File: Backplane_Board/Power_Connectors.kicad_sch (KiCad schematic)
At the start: 15 parts, among them J1 Conn_01x02_Pin, J10 Conn_01x02_Pin, J11 Conn_01x02_Pin, J12 Conn_01x02_Pin, J13 Conn_01x02_Pin, J14 Conn_01x02_Pin, J15 Conn_01x02_Pin, J16 Conn_01x02_Pin, J2 Conn_01x02_Pin, J4 Conn_01x02_Pin, J5 Conn_01x02_Pin, J6 Conn_01x02_Pin, J7 Conn_01x02_Pin, J8 Conn_01x02_Pin, J9 Conn_01x02_Pin

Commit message: add rerevised esc board and rough backplane schmatic
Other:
- company: (none) -> Cabrillo Robtics
- title: (none) -> Backplane_Board
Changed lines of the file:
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@@
 	(generator_version "8.0")
 	(paper "A4")
+	(title_block
+		(title "Backplane_Board")
+		(date "2024-09-30")
+		(rev "1")
+		(company "Cabrillo Robtics")
+		(comment 1 "LaserShark Backplane PCB")
+	)
 	(wire
 		(pts

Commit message: back plane board ready for review
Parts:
- added C11, C7, C8: 330 uF, 220UF CAP:CAP_16SVPG330MX, symbol Device:C_Polarized_Small_US
- added D3: LED, symbol Device:LED
- added J18, J19, J20, J3: Conn_01x02_Pin, symbol Connector:Conn_01x02_Pin
- added R10, R15: DNP, symbol Device:R
- added R17: 10K, symbol Device:R
- added U6: PKU3511SPI, PKU 3500S_FPM, symbol PKU3511SPI:PKU3511SPI
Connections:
- net +12V: now also J3.2 (Pin_2), U6.1 (+VIN)
- net +5V: now also C11.1, C7.1, C8.1, D3.2 (A), J18.2 (Pin_2), J19.2 (Pin_2), J20.2 (Pin_2), R10.1, U6.7 (SENSE), U6.8 (+VO)
- net GND: now also C11.2, C7.2, C8.2, J18.1 (Pin_1), J19.1 (Pin_1), J20.1 (Pin_1), J3.1 (Pin_1), R15.2, R17.2, U6.2 (ON/OFF), U6.3 (-VIN), U6.4 (-VO), U6.5 (SENSE)
- new net: R10.2, R15.1, U6.6 (TRIM)
- new net: D3.1 (K), R17.1
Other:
- note added: "12V Clean Power Bus External Power Connections"
- note added: "12V ESC Power Bus External Power Connections"
- note added: "5V Power Bus"
- note added: "5V Power Bus Cap Banks and status LEDs"
- note added: "5V Power Bus External Power Connections"
- note added: "Input Test Accesses"
- note added: "fuse?"
- note removed: "This bus is used to power anything that could be dangrous things go crazy ESC Boards, Tooling..."
- moved on the sheet: J1, J11, J16, J2, J4, J5, J6

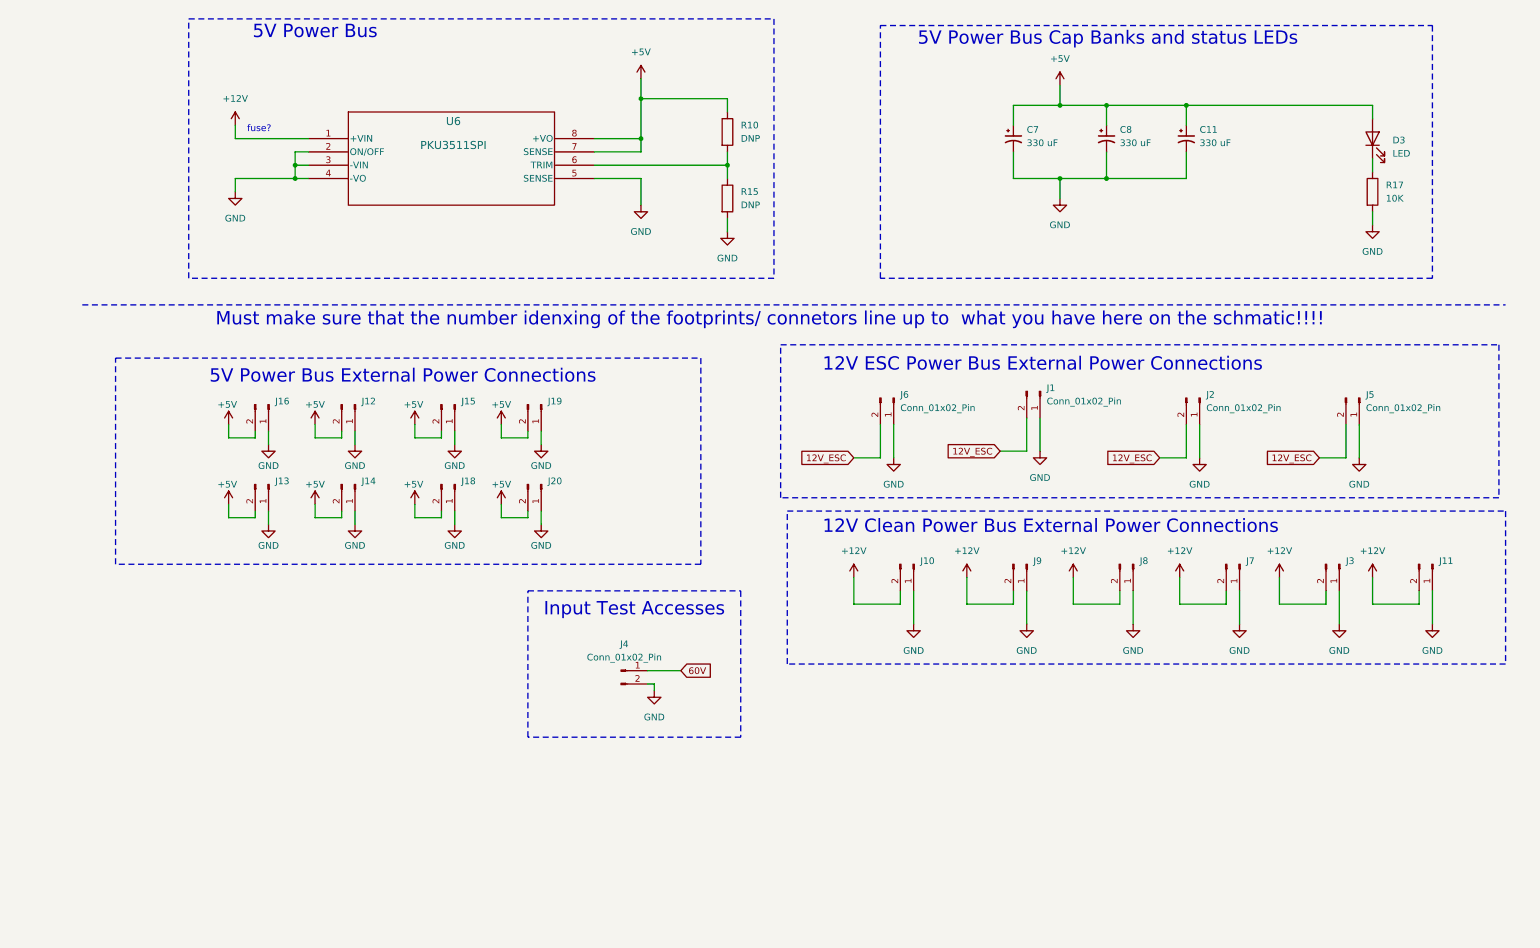
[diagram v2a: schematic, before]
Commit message: added pico and 5v killSW
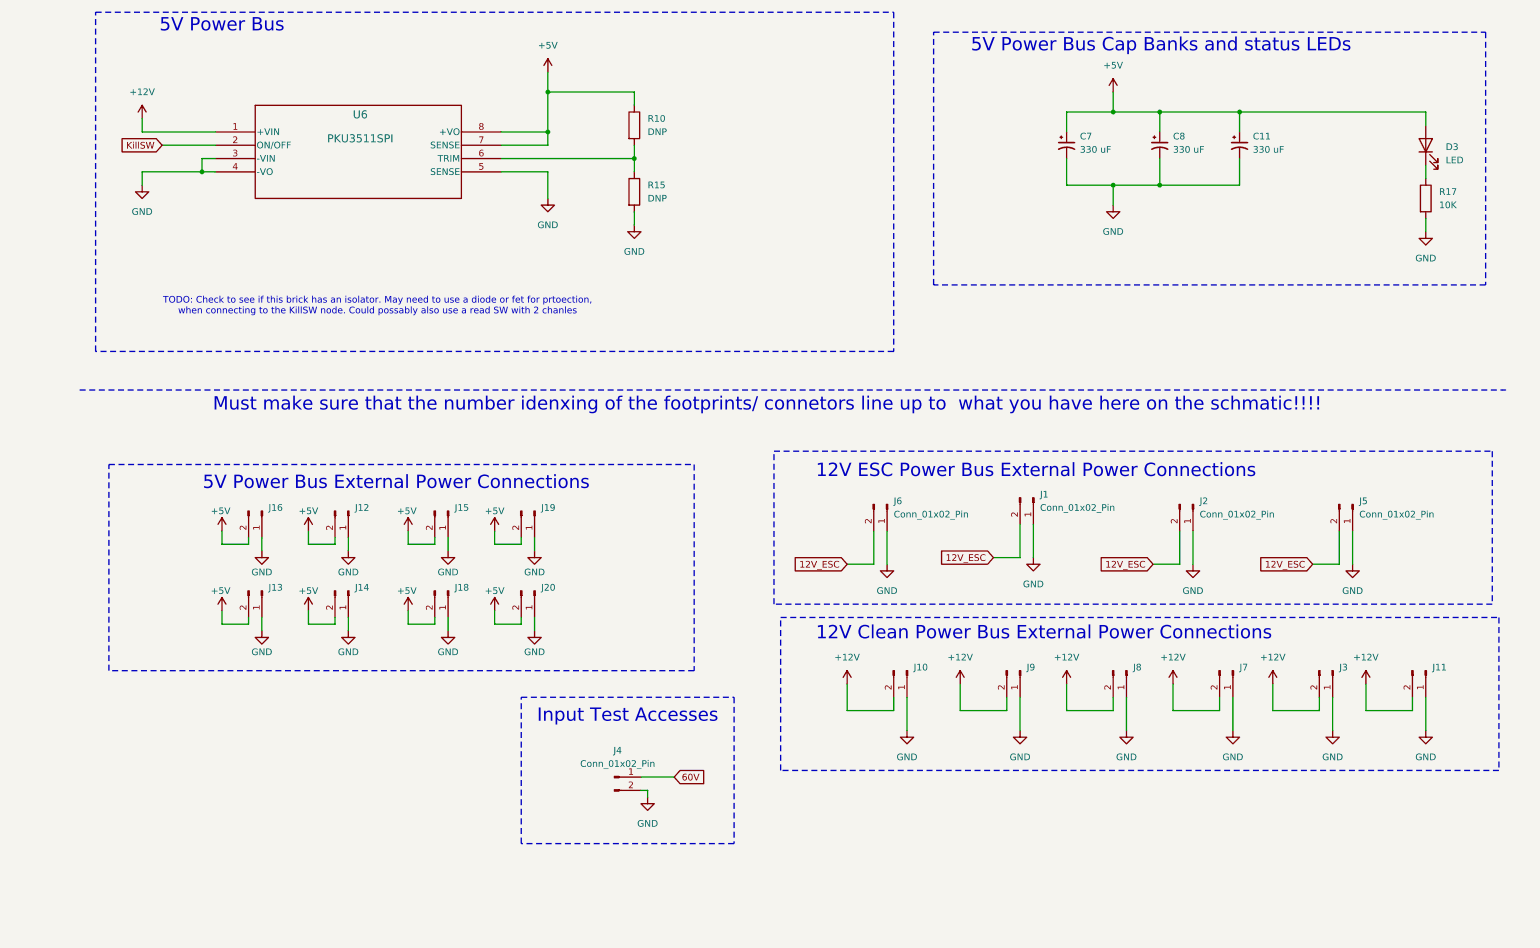
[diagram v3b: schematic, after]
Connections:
- net GND: no longer U6.2 (ON/OFF)
- new net KillSW: U6.2 (ON/OFF)
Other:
- note added: "TODO: Check to see if this brick has an isolator. May need to use a diode or fet for prtoection, when connecting to the KillSW node. Could possably also use a read SW with 2 chanles"
- note removed: "fuse?"
- moved on the sheet: C11, C7, C8, D3, J1, J10, J11, J12, J13, J14, J15, J16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

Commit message: added more pico stuff
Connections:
- net KillSW is gone; now on net GND: U6.2 (ON/OFF)
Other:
- note added: "TODO: Check to see if this brick has an isolator. May need to use a diode or fet for prtoection, when connecting to the KillSW node. Could possably also use a read SW with 2 chanles Note: Currently aways on. We do not want to kill the full buss in the event that the kill swtich is pulled"
- note removed: "TODO: Check to see if this brick has an isolator. May need to use a diode or fet for prtoection, when connecting to the KillSW node. Could possably also use a read SW with 2 chanles"
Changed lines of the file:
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@@
+	)
+	(junction
+		(at 35.56 41.91)
+		(diameter 0)
+		(color 0 0 0 0)
 	)
 	(junction
@@
 	(wire
 		(pts
+			(xy 35.56 39.37) (xy 35.56 41.91)
+		)
+		(stroke
+			(width 0)
+			(type default)
+		)
+	)
+	(wire
+		(pts
 			(xy 44.45 130.81) (xy 44.45 129.54)
+		)
+		(stroke
+			(width 0)
+			(type default)
+		)
+	)
+	(wire
+		(pts
+			(xy 38.1 39.37) (xy 35.56 39.37)
 		)
 		(stroke
@@
 		(pts
 			(xy 269.24 53.34) (xy 269.24 55.88)
-		)
-		(stroke
-			(width 0)
-			(type default)
-		)
-	)
-	(wire
-		(pts
-			(xy 27.94 39.37) (xy 38.1 39.37)
 		)
 		(stroke
@@
 		)
 	)
-	(text "TODO: Check to see if this brick has an isolator. May need to use a diode or fet for prtoection,\nwhen connecting to the KillSW node. Could possably also use a read SW with 2 chanles"
+	(text "TODO: Check to see if this brick has an isolator. May need to use a diode or fet for prtoection,\nwhen connecting to the KillSW node. Could possably also use a read SW with 2 chanles\n\nNote: Currently aways on. We do not want to kill the full buss in the event that the kill swtich is pulled"
 		(exclude_from_sim no)
-		(at 69.088 70.104 0)
+		(at 45.212 68.58 0)
 		(effects
 			(font
@@
 				(color 255 52 89 1)
 			)
+			(justify left)
 		)
 	)
@@
 			(effects
 				(font
-					(size 1.27 1.27)
-				)
-				(justify right)
-				(hide yes)
-			)
-		)
-	)
-	(global_label "KillSW"
-		(shape input)
-		(at 27.94 39.37 180)
-		(fields_autoplaced yes)
-		(effects
-			(font
-				(size 1.27 1.27)
-			)
-			(justify right)
-		)
-		(property "Intersheetrefs" "${INTERSHEET_REFS}"
-			(at 19.0887 39.37 0)
-			(effects
-				(font

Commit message: ready for final schmatic review
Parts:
- R10, R15: now not fitted
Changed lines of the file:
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@@
 		(in_bom yes)
 		(on_board yes)
-		(dnp no)
+		(dnp yes)
 		(fields_autoplaced yes)
 		(property "Reference" "R15"
@@
 		(in_bom yes)
 		(on_board yes)
-		(dnp no)
+		(dnp yes)
 		(fields_autoplaced yes)
 		(property "Reference" "R10"

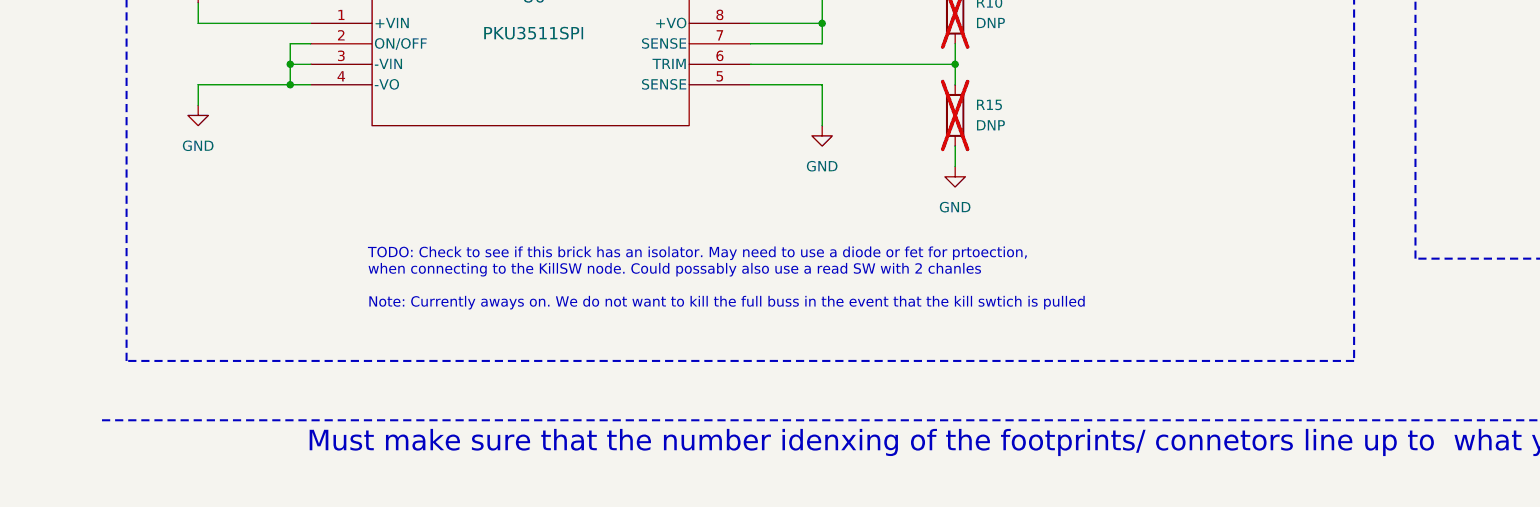
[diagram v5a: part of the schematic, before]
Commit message: updated i2c pullups to 3V3 logic, not isolator needed
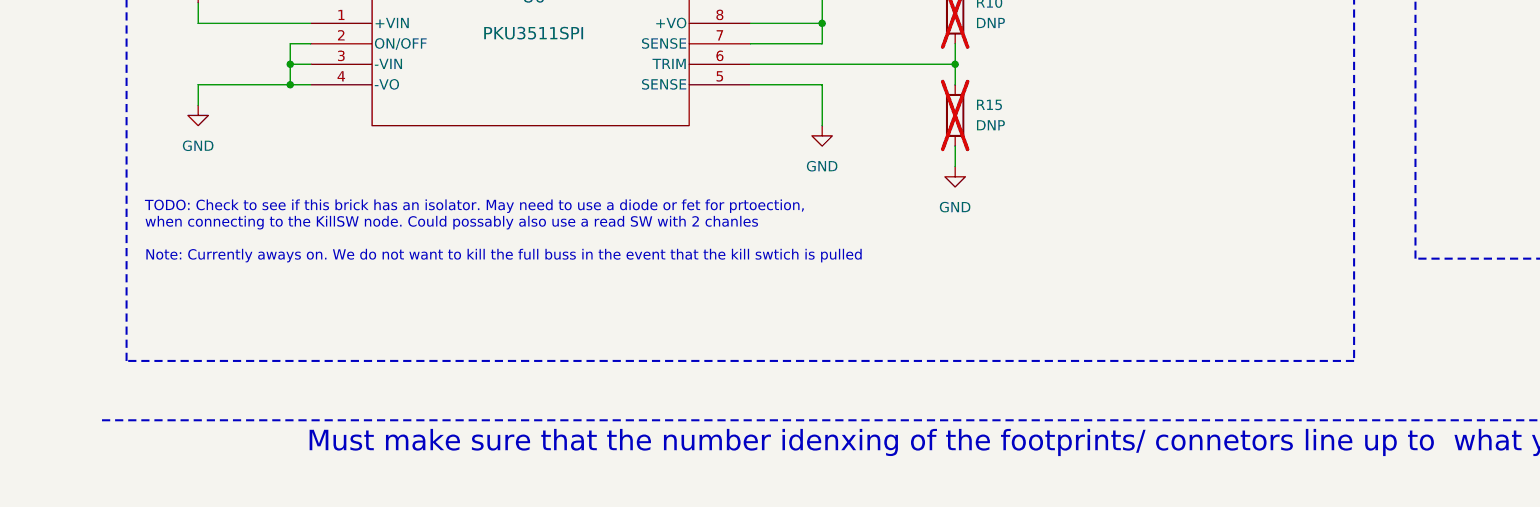
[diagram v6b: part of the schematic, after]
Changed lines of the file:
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@@
 	(text "TODO: Check to see if this brick has an isolator. May need to use a diode or fet for prtoection,\nwhen connecting to the KillSW node. Could possably also use a read SW with 2 chanles\n\nNote: Currently aways on. We do not want to kill the full buss in the event that the kill swtich is pulled"
 		(exclude_from_sim no)
-		(at 45.212 68.58 0)
+		(at 17.526 62.738 0)
 		(effects
 			(font

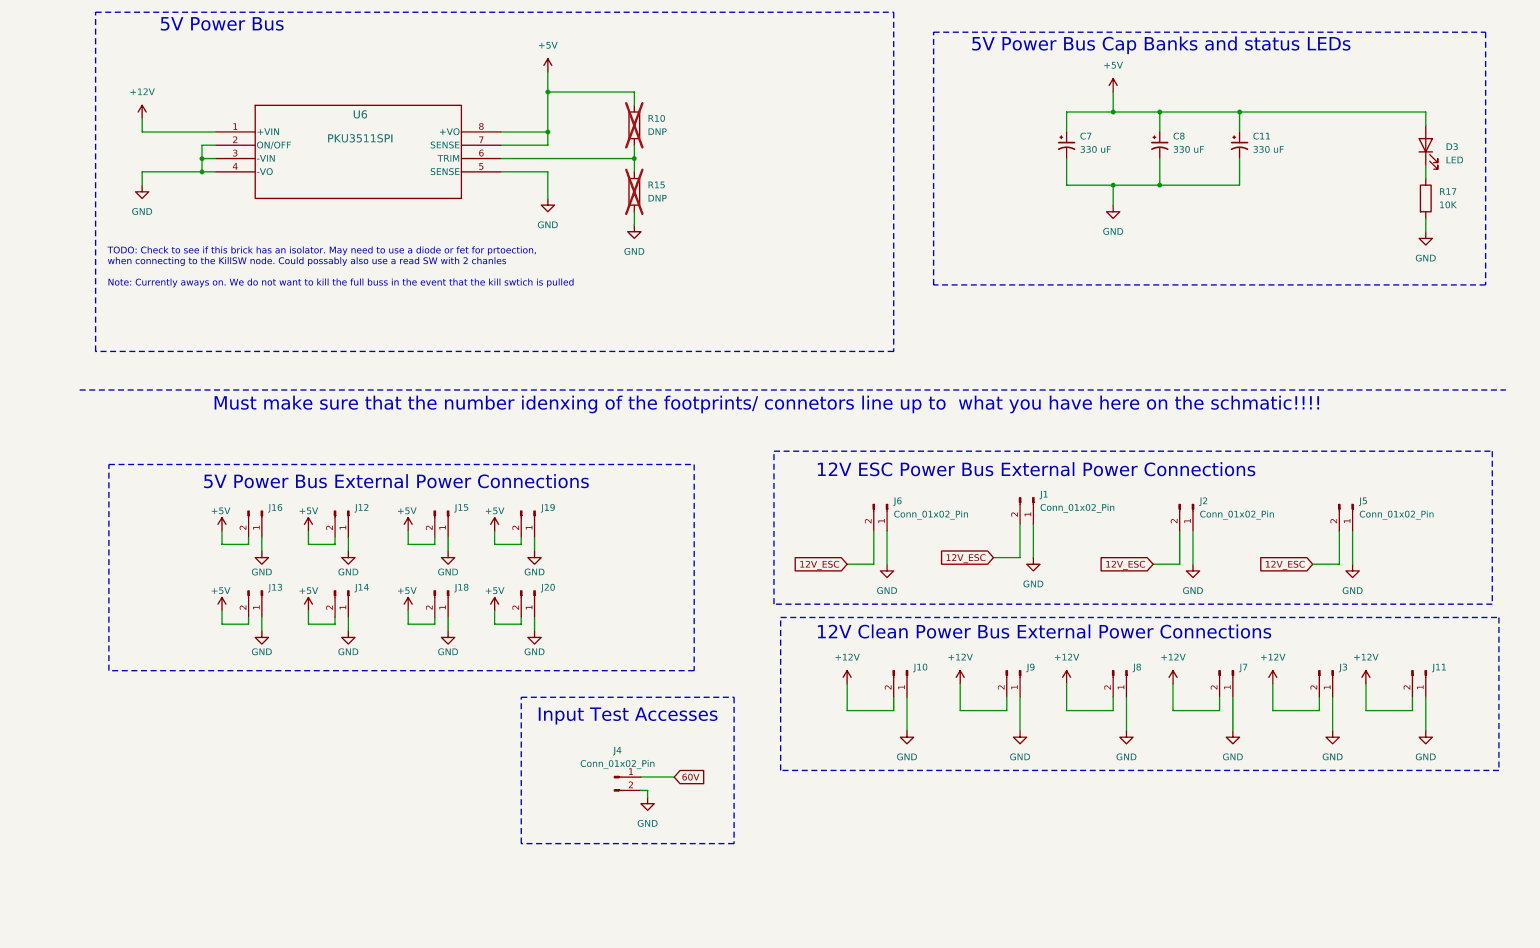
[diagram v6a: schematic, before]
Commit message: update FET circits
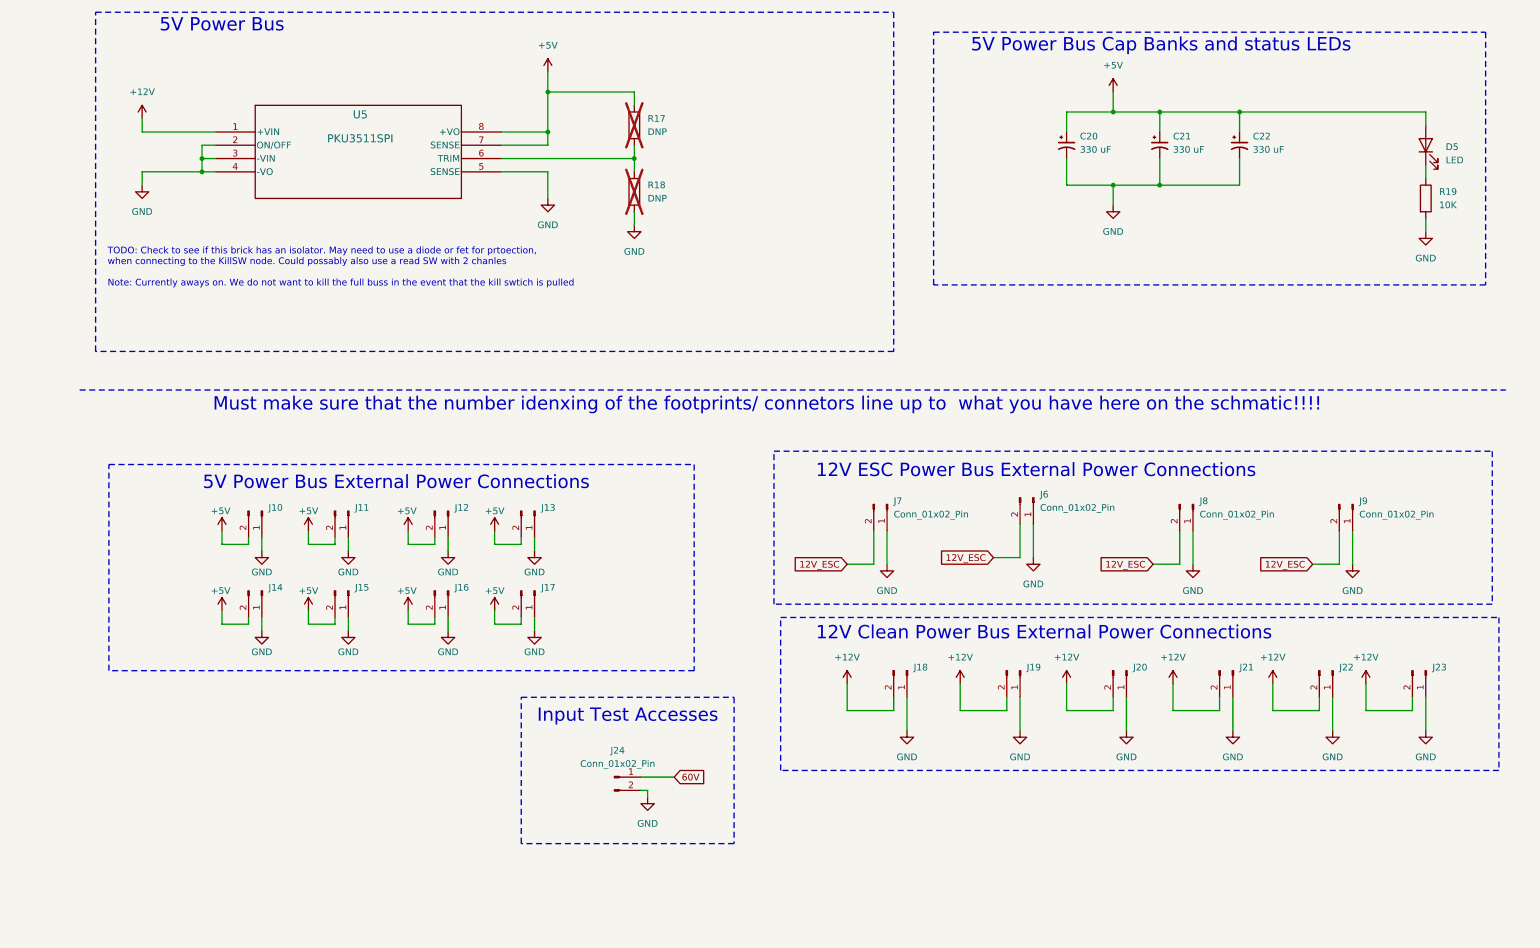
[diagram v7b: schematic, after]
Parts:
- renumbered C7 to C20, C8 to C21, C11 to C22, D3 to D5, J16 to J10, J12 to J11, J15 to J12, J19 to J13, J13 to J14, J14 to J15, J18 to J16, J20 to J17, J10 to J18, J9 to J19, J8 to J20, J7 to J21, J3 to J22, J11 to J23, J4 to J24, J1 to J6, J6 to J7, J2 to J8, J5 to J9, R10 to R17, R15 to R18, R17 to R19, U6 to U5
